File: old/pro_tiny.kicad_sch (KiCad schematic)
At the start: 28 parts, among them J1 Connector 1x12, J2 Connector 1x12, J3 Conn_01x05, J4 USB-C 2.0 mid-mount female co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, U1 ATmega32U4-M, Y1 Crystal_GND24_Small

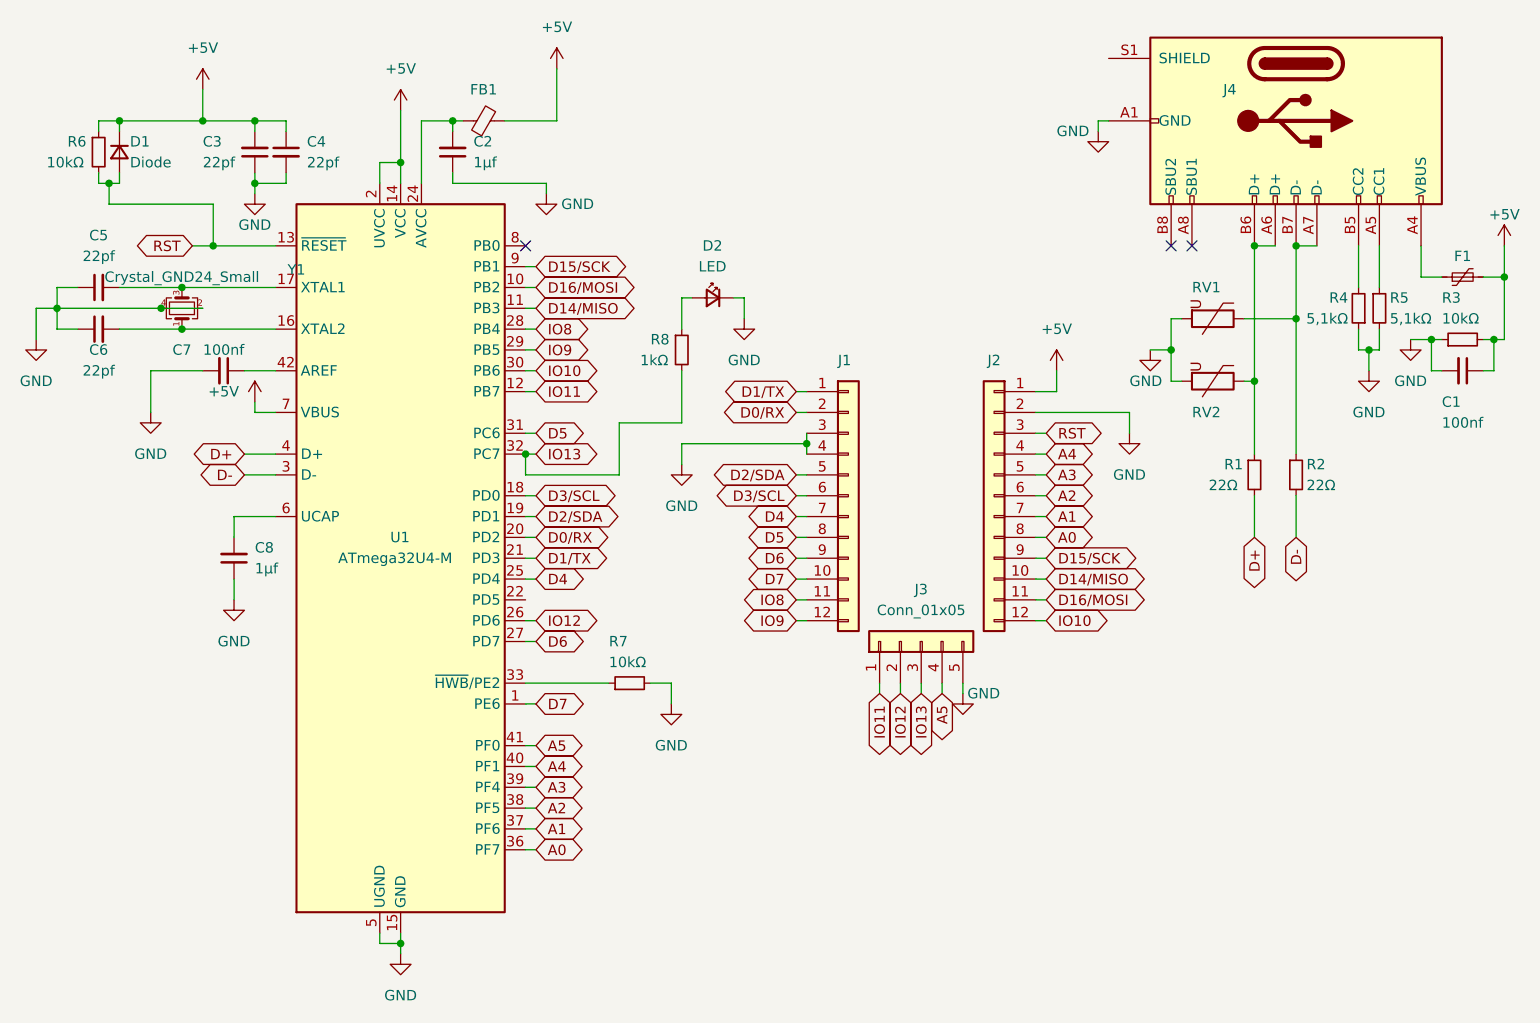
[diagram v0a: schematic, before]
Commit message: fixed some dumb missed connection
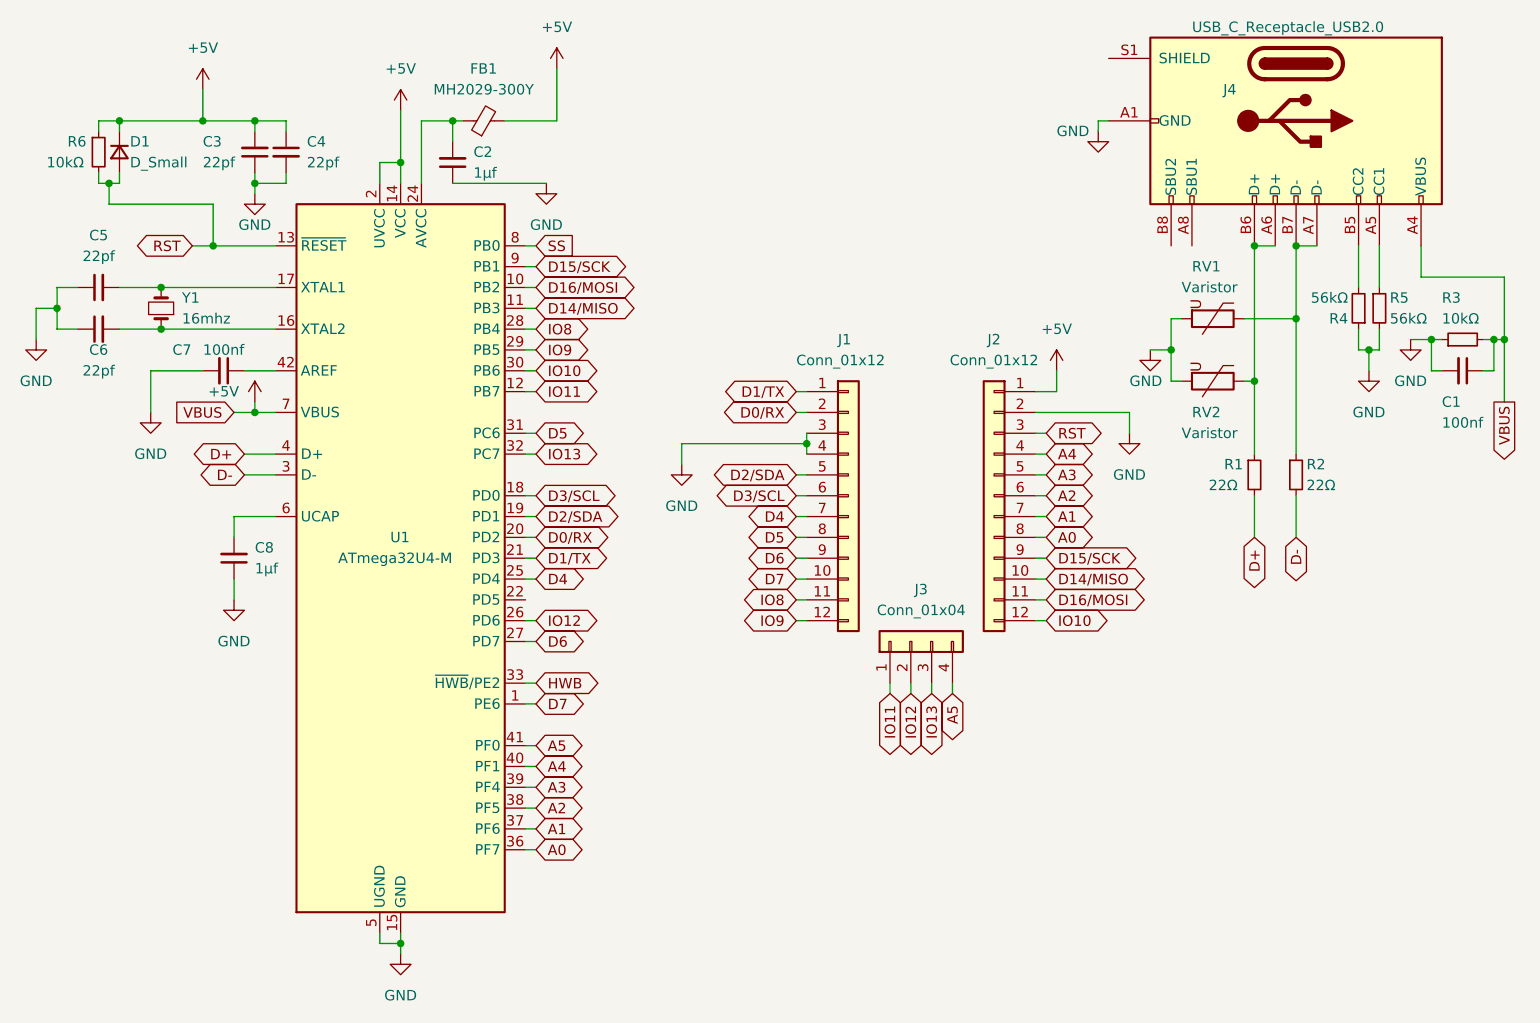
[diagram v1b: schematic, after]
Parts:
- removed D2: LED, LED_SMD:LED_0402_1005Metric, symbol Device:LED_Small
- removed F1: Polyfuse 500mA HC, Fuse:Fuse_0402_1005Metric, symbol Device:Polyfuse_Small
- removed J3: Conn_01x05, Connector_PinHeader_1.27mm:PinHeader_1x05_P1.27mm_Vertical, symbol Connector_Generic:Conn_01x05
- removed R7: 10kΩ, Resistor_SMD:R_0402_1005Metric, symbol Device:R_Small
- removed R8: 1kΩ, Resistor_SMD:R_0402_1005Metric, symbol Device:R_Small
- removed Y1: Crystal_GND24_Small, Crystal:Crystal_SMD_2016-4Pin_2.0x1.6mm, symbol Device:Crystal_GND24_Small
- added J3: Conn_01x04, Connector_PinHeader_1.27mm:PinHeader_1x04_P1.27mm_Vertical, symbol Connector_Generic:Conn_01x04
- added Y1: 16mhz, Crystal:Crystal_SMD_2016-4Pin_2.0x1.6mm, symbol Device:Crystal_Small
- D1: value Diode -> D_Small
- FB1: value Ferrite bead low-pass filter -> MH2029-300Y
- J1, J2: value Connector 1x12 -> Conn_01x12
- J4: value USB-C 2.0 mid-mount female connector -> USB_C_Receptacle_USB2.0
- R4, R5: value 5,1kΩ -> 56kΩ
- RV1, RV2: value ESD protection varistor -> Varistor
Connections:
- net +5V: now also J4.A4 (VBUS), J4.A9 (VBUS), J4.B4 (VBUS), J4.B9 (VBUS)
- net A5: now also J3.4 (Pin_4)
- net IO11: now also J3.1 (Pin_1)
- net IO12: now also J3.2 (Pin_2)
- net IO13: now also J3.3 (Pin_3)
- net at C6.2, U1.16 (XTAL2): now also Y1.1
- net at C5.2, U1.17 (XTAL1): now also Y1.2
- net HWB: now reaches U1.33 (~{HWB}/PE2)
- net SS: now reaches U1.8 (PB0)
- no-connect marks 3 -> 0
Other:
- company: Rasmus L. -> (none)
- title: "Epi" -> "Pro Tiny"
- moved on the sheet: C2
